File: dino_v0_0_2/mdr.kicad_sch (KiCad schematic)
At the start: 16 parts, among them U18 74LS373, U22 74LS02, U25 74LS245, U34 74LS373, U37 74LS04, U39 74LS00, U72 74LS245, U73 74LS245

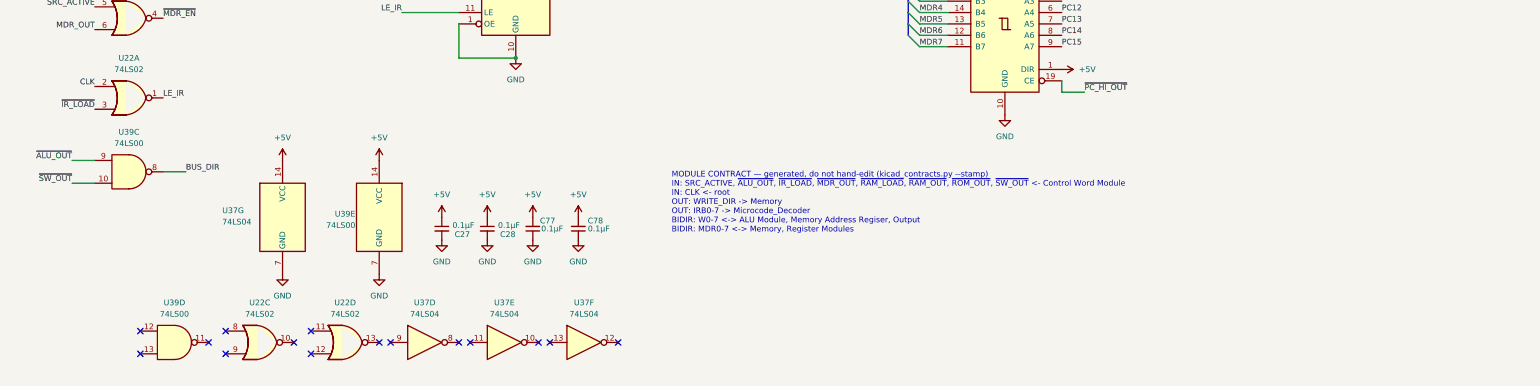
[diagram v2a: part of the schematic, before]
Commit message: feat: phase D on silicon — the machine executes from RAM
PROG_ramexec returns 0x6E. The PC has been above 0x7FFF and FETCH_RAM has
been high, both for the first time in this machine's life.

The missing condition was never "is this a fetch." ~ROM_OUT is asserted for
every src=ROM — opcode fetch, LDAI's immediate, LDA/STA/JMP/CALL operand
bytes — so an instruction living in RAM must read its operands from RAM
too. The condition is "a ROM-side read was requested, but the address is
above 0x7FFF":

    FETCH_RAM = NOR(~ROM_OUT, ~RAM_EN)

Six gate sections, no new IC. All six were free on U22/U37/U39, already in
sockets on the MDR board, where ~ROM_OUT and ~RAM_OUT already sit feeding
READS_IDLE. Only ~RAM_EN had to be brought in.

    U22 g3   FETCH_RAM     = NOR(~ROM_OUT, ~RAM_EN)
    U22 g4   ROM_BUF_ON    = NOR(~ROM_OUT, FETCH_RAM)
    U37 inv4 ~{FETCH_RAM}
    U37 inv6 ~{ROM_BUF_EN} = OR(~ROM_OUT, FETCH_RAM)   -> U19.19
    U37 inv5 ~{RAM_OE_G}   = AND(~RAM_OUT, ~FETCH_RAM) -> U26.22 + U51.9
    U39 g4   RAM_OE_ON     = NAND(~RAM_OUT, ~FETCH_RAM)

Two pin lifts on the memory board, eleven wires. U24.22 stays on ~ROM_OUT:
U24's own ~CE = M15 already deselects the ROM chip at RAM addresses.

Gating ~RAM_OUT upstream is what keeps this at six gates rather than eight.
U51 is a 7400 computing ~RAM_MDR_EN = AND(~RAM_OUT, ~WRITE_DIR), so one
gate on ~RAM_OUT moves both the RAM chip's ~OE and its buffer's ~CE.

Re-proved before building: all 15 src=ROM microcode rows carry mux_pc=True,
FETCH included, and FILL is src=NONE. A ROM-side read can now land in RAM,
so the standing "ROM reads are exempt from the src=RAM -> MAR loop" rule was
no longer free. It holds — MAR never drives M during a ROM-side read, and a
runaway opcode cannot open the loop either.

The witness is not permutation-blind. If the fetch had still come from ROM,
PC=0x9000 presents A0-A14 = 0x1000 to U24, which is 0xFF fill, which is
HALT, so the poison would have survived as 0xFF. 0x6E is 0x8B - 0x1D,
compu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
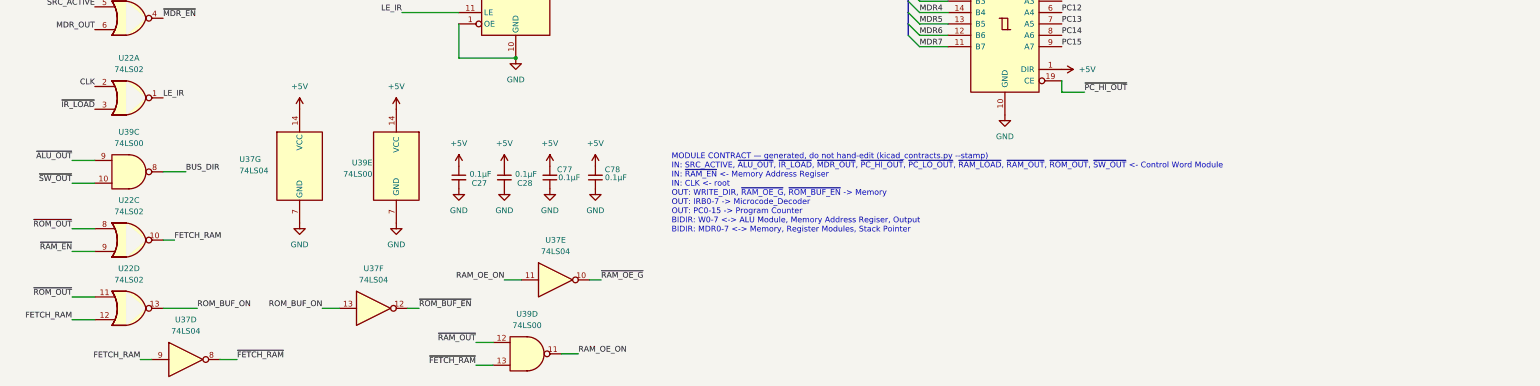
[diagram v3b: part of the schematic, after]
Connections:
- net ~{RAM_OUT}: now also U39.12
- net ~{ROM_OUT}: now also U22.11, U22.8
- net RAM_OE_ON: now reaches U39.11
- net RAM_OE_ON: now also U37.11
- net ~{FETCH_RAM}: now reaches U39.13
- net ~{FETCH_RAM}: now also U37.8
- net FETCH_RAM: now reaches U22.12
- net FETCH_RAM: now also U22.10, U37.9
- net ROM_BUF_ON: now reaches U22.13
- net ROM_BUF_ON: now also U37.13
- net ~{RAM_EN}: now reaches U22.9
- net ~{RAM_OE_G}: now reaches U37.10
- net ~{ROM_BUF_EN}: now reaches U37.12
- no-connect marks 15 -> 0
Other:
- note added: "MODULE CONTRACT — generated, do not hand-edit (kicad_contracts.py --stamp) IN: SRC_ACTIVE, ~{ALU_OUT}, ~{IR_LOAD}, ~{MDR_OUT}, ~{PC_HI_OUT}, ~{PC_LO_OUT}, ~{RAM_LOAD}, ~{RAM_OUT}, ~{ROM_OUT}, ~{SW_OUT} <- Control Word Module IN: ~{RAM_EN} <- Memory Address Regiser IN: CLK <- root OUT: WRITE_DIR, ~{RAM_OE_G}, ~{ROM_BUF_EN} -> Memory OUT: IRB0-7 -> Microcode_Decoder OUT: PC0-15 -> Program Counter B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"
- note removed: "MODULE CONTRACT — generated, do not hand-edit (kicad_contracts.py --stamp) IN: SRC_ACTIVE, ~{ALU_OUT}, ~{IR_LOAD}, ~{MDR_OUT}, ~{RAM_LOAD}, ~{RAM_OUT}, ~{ROM_OUT}, ~{SW_OUT} <- Control Word Module IN: CLK <- root OUT: WRITE_DIR -> Memory OUT: IRB0-7 -> Microcode_Decoder BIDIR: W0-7 <-> ALU Module, Memory Address Regiser, Output BIDIR: MDR0-7 <-> Memory, Register Modules"
- moved on the sheet: C27, C28, C77, C78, U22C, U22D, U37D, U37E, U37F, U37G, U39D, U39E

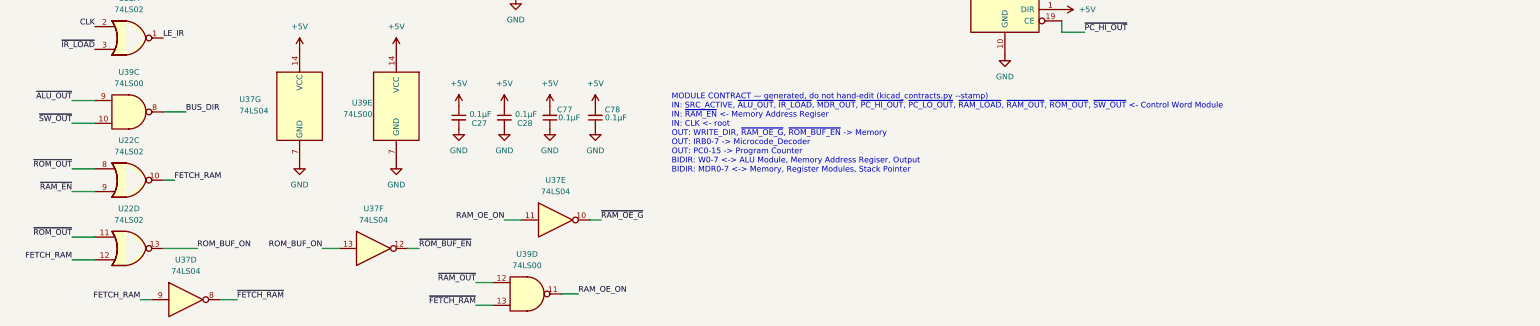
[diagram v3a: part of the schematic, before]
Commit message: feat: phase E step A -- the 16K I/O window, in schematic
Carves 0x4000-0x7FFF out of ROM space and publishes a bus. The ROM now
answers 0x0000-0x3FFF only; the window decodes to no core chip, so W
reads its park -- 0xFF, which is HALT.

TWO NEW PACKAGES, both on the memory board:

  U74 '00  ~{M14}      = NAND(M14, M14)
           ~{ROM_SEL}  = NAND(~{RAM_EN}, ~{M14})
           ~{RAM_OE_G} = NAND(RAM_OE_ON, M15)
           ~{IO_SEL}   = NAND(~{RAM_EN}, M14)
  U75 '32  ~{IO_RD}    = OR(~{IO_SEL}, READS_IDLE)
           ~{IO_WR}    = OR(~{IO_SEL}, ~{RAM_WRITE_EN})
           RESET_B     = OR(RESET, GND)
           ~{IO_RD_Q}  = OR(~{IO_RD}, CLK)

Eight copper changes: U24.20 and U22.12 to ~{ROM_SEL}, U26.22/U51.9 fed
from U74 g3, U39.10 to ~{IO_RD}, U37.10 and U28.7 unlanded, U37.11 to
GND. Park: R4-R8 + R25-R27, 4.7k on W0-7. CLK crosses through R3, 100R,
source end -- the R2 treatment.

IN RETIRES. ~{SW_OUT} has zero pins project-wide. SWITCH-GATE1's enables
are strapped +5V until card zero drives them from an address decode.

THE ROM_EN ALIAS IS DELETED. Once U24.20 moved, ROM_EN named a net with
no ROM consumer. Deleting it half-way SPLIT the net and alias_splits()
caught it mid-edit -- M15: ['M15', 'M15/ROM_EN'], the exact two-key
failure that once cost this project the ROM chip-enable on every
continuity checklist ever generated.

CLK WAS A FOURTH CROSSING THE SPEC DID NOT CARRY. Census: 15 CLK pins,
none on the memory board; ~{CLK} at U51.4 is the wrong polarity and both
new packages are full. SECTION 1's cost table predated the read-term
split that spent U75 g4, so memory is +4 and MDR is +4 -- the wire margin
is zero. Ruled: stay on memory, the output-load argument still holds.

SWITCH-GATE1/SW1/R17-R24/C48 move to their own input.kicad_sch so the
DIP card is modelled as a card. No renumbering: 168 designators
unchanged, --since reports annotate=0.

TOOLING RECONCILED TO THE DESIGN, not the reverse:
  test_continuity_completeness  M15_PINS U24.20 -> U74.10; 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
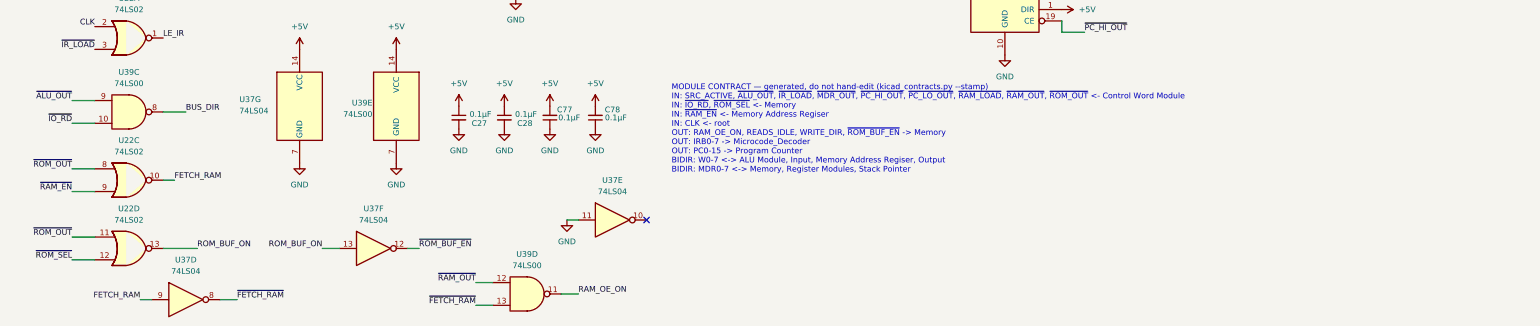
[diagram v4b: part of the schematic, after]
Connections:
- net FETCH_RAM: no longer U22.12
- net GND: now also U37.11
- net RAM_OE_ON: no longer U37.11
- net ~{RAM_OE_G}: no longer names the net of U37.10
- net ~{SW_OUT} renamed ~{IO_RD}
- new net ~{ROM_SEL}: U22.12
- no-connect marks 0 -> 1
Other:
- note added: "MODULE CONTRACT — generated, do not hand-edit (kicad_contracts.py --stamp) IN: SRC_ACTIVE, ~{ALU_OUT}, ~{IR_LOAD}, ~{MDR_OUT}, ~{PC_HI_OUT}, ~{PC_LO_OUT}, ~{RAM_LOAD}, ~{RAM_OUT}, ~{ROM_OUT} <- Control Word Module IN: ~{IO_RD}, ~{ROM_SEL} <- Memory IN: ~{RAM_EN} <- Memory Address Regiser IN: CLK <- root OUT: RAM_OE_ON, READS_IDLE, WRITE_DIR, ~{ROM_BUF_EN} -> Memory OUT: IRB0-7 -> Microcode_Decode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"
- note removed: "MODULE CONTRACT — generated, do not hand-edit (kicad_contracts.py --stamp) IN: SRC_ACTIVE, ~{ALU_OUT}, ~{IR_LOAD}, ~{MDR_OUT}, ~{PC_HI_OUT}, ~{PC_LO_OUT}, ~{RAM_LOAD}, ~{RAM_OUT}, ~{ROM_OUT}, ~{SW_OUT} <- Control Word Module IN: ~{RAM_EN} <- Memory Address Regiser IN: CLK <- root OUT: WRITE_DIR, ~{RAM_OE_G}, ~{ROM_BUF_EN} -> Memory OUT: IRB0-7 -> Microcode_Decoder OUT: PC0-15 -> Program Counter B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"
- moved on the sheet: U37E
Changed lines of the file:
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@@
 		(color 0 0 0 0)
 	)
+	(no_connect
+		(at 153.67 181.61)
+	)
 	(bus_entry
 		(at 214.63 111.76)
@@
 	(wire
 		(pts
-			(xy 125.73 181.61) (xy 121.92 181.61)
-		)
-		(stroke
-			(width 0)
-			(type default)
-		)
-	)
-	(wire
-		(pts
 			(xy 125.73 26.67) (xy 90.17 26.67)
 		)
@@
 	(wire
 		(pts
-			(xy 140.97 181.61) (xy 143.51 181.61)
-		)
-		(stroke
-			(width 0)
-			(type default)
-		)
-	)
-	(wire
-		(pts
 			(xy 107.95 114.3) (xy 111.76 114.3)
 		)
@@
 	(wire
 		(pts
+			(xy 135.89 181.61) (xy 138.43 181.61)
+		)
+		(stroke
+			(width 0)
+			(type default)
+		)
+	)
+	(wire
+		(pts
 			(xy 107.95 46.99) (xy 119.38 46.99)
 		)
@@
 		)
 	)
-	(label "~{SW_OUT}"
+	(label "~{IO_RD}"
 		(at 25.4 160.02 180)
 		(effects
@@
 		)
 	)
-	(label "FETCH_RAM"
+	(label "~{ROM_SEL}"
 		(at 25.4 190.5 180)
 		(effects
@@
 		)
 	)
-	(label "RAM_OE_ON"
-		(at 121.92 181.61 180)
-		(effects
-			(font
-				(size 1.27 1.27)
-			)
-			(justify right bottom)
-		)
-	)
 	(label "~{RAM_LOAD}"
 		(at 30.48 66.04 180)
@@
 		)
 	)
-	(label "~{RAM_OE_G}"
-		(at 143.51 181.61 0)
-		(effects
-			(font
-				(size 1.27 1.27)
-			)
-			(justify left bottom)
-		)
-	)
 	(label "MDR4"
 		(at 214.63 121.92 0)
@@
 	(symbol
 		(lib_id "74xx:74LS04")
-		(at 133.35 181.61 0)
+		(at 146.05 181.61 0)
 		(unit 5)
 		(body_style 1)
@@
 		(fields_autoplaced yes)
 		(property "Reference" "U37"
-			(at 133.35 172.72 0)
+			(at 146.05 172.72 0)
 			(show_name no)
 			(do_not_autoplace no)
@@
 		)
 		(property "Value" "74LS04"
-			(at 133.35 175.26 0)
+			(at 146.05 175.26 0)
 			(show_name no)
 			(do_not_autoplace no)
@@
 		)
 		(property "Footprint" ""
-			(at 133.35 181.61 0)
+			(at 146.05 181.61 0)
 			(hide yes)
 			(show_name no)
@@
 		)
 		(property "Datasheet" "http://www.ti.com/lit/gpn/sn74LS04"
-			(at 133.35 181.61 0)
+			(at 146.05 181.61 0)
 			(hide yes)
 			(show_name no)
@@
 		)
 		(property "Description" "Hex Inverter"
-			(at 133.35 181.61 0)
+			(at 146.05 181.61 0)
 			(hide yes)
 			(show_name no)
@@
 	)
 	(symbol
+		(lib_id "power:GND")
+		(at 135.89 181.61 0)
+		(mirror y)
+		(unit 1)
+		(body_style 1)
+		(exclude_from_sim no)
+		(in_bom yes)
+		(on_board yes)
+		(in_pos_files yes)
+		(dnp no)
+		(property "Reference" "#PWR0225"
+			(at 135.89 187.96 0)
+			(hide yes)
+			(show_name no)
+			(do_not_autoplace no)
+			(effects
+				(font
+					(size 1.27 1.27)
+				)
+			)
+		)
+		(property "Value" "GND"
+			(at 135.89 186.436 0)
+			(show_name no)
+			(do_not_autoplace no)
+			(effects
+				(font
+					(size 1.27 1.27)
+				)
+			)
+		)
+		(property "Footprint" ""
+			(at 135.89 181.61 0)
+			(hide yes)
+			(show_name no)
+			(do_not_autoplace no)
+			(effects
+				(font
+					(size 1.27 1.27)
+				)
+			)
+		)
+		(property "Datasheet" ""
+			(at 135.89 181.61 0)
+			(hide yes)
+			(show_name no)
+			(do_not_autoplace no)
+			(effects
+				(font
+					(size 1.27 1.27)
+				)
+			)
+		)
+		(property "Description" "Power symbol creates a global label with name \"GND\" , ground"
+			(at 135.89 181.61 0)
+			(hide yes)
+			(show_name no)
+			(do_not_autoplace no)
+			(effects
+				(font
+					(size 1.27 1.27)
+				)
+			)
+		)
+		(pin "1"
+		)
+		(instances
+			(project "dino_v0_0_2"
+				(path "/e43166a5-d972-471d-b3cf-9f4f12c7f541/dfdf99e6-2845-4ba5-89ea-a5852382fb95"
+					(reference "#PWR0225")
+					(unit 1)
+				)
+			)
+		)
+	)
+	(symbol
 		(lib_id "74xx:74LS04")
 		(at 38.1 106.68 0)
@@
 		)
 	)
-	(text "MODULE CONTRACT — generated, do not hand-edit (kicad_contracts.py --stamp)\nIN: SRC_ACTIVE, ~{ALU_OUT}, ~{IR_LOAD}, ~{MDR_OUT}, ~{PC_HI_OUT}, ~{PC_LO_OUT}, ~{RAM_LOAD}, ~{RAM_OUT}, ~{ROM_OUT}, ~{SW_OUT} <- Control Word Module\nIN: ~{RAM_EN} <- Memory Address Regiser\nIN: CLK <- root\nOUT: WRITE_DIR, ~{RAM_OE_G}, ~{ROM_BUF_EN} -> Memory\nOUT: IRB0-7 -> Microcode_Decoder\nOUT: PC0-15 -> Program Counter\nBIDIR: W0-7 <-> ALU Module, Memory Address Regiser, Output\nBIDIR: MDR0-7 <-> Memory, Register Modules, Stack Pointer"
+	(text "MODULE CONTRACT — generated, do not hand-edit (kicad_contracts.py --stamp)\nIN: SRC_ACTIVE, ~{ALU_OUT}, ~{IR_LOAD}, ~{MDR_OUT}, ~{PC_HI_OUT}, ~{PC_LO_OUT}, ~{RAM_LOAD}, ~{RAM_OUT}, ~{ROM_OUT} <- Control Word Module\nIN: ~{IO_RD}, ~{ROM_SEL} <- Memory\nIN: ~{RAM_EN} <- Memory Address Regiser\nIN: CLK <- root\nOUT: RAM_OE_ON, READS_IDLE, WRITE_DIR, ~{ROM_BUF_EN} -> Memory\nOUT: IRB0-7 -> Microcode_Decoder\nOUT: PC0-15 -> Program Counter\nBIDIR: W0-7 <-> ALU Module, Input, Memory Address Regiser, Output\nBIDIR: MDR0-7 <-> Memory, Register Modules, Stack Pointer"
 		(exclude_from_sim no)
 		(at 159.258 171.196 0)
